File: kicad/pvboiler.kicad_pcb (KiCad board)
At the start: 2 copper layers, 125 x 60 mm, 52 parts, among them J1 Conn_01x04, J2 Screw_Terminal_01x04, J3 Conn_01x04, J4 Screw_Terminal_01x03, U1 MOC3021M, U2 H11AA1, U3 IRM-03-5

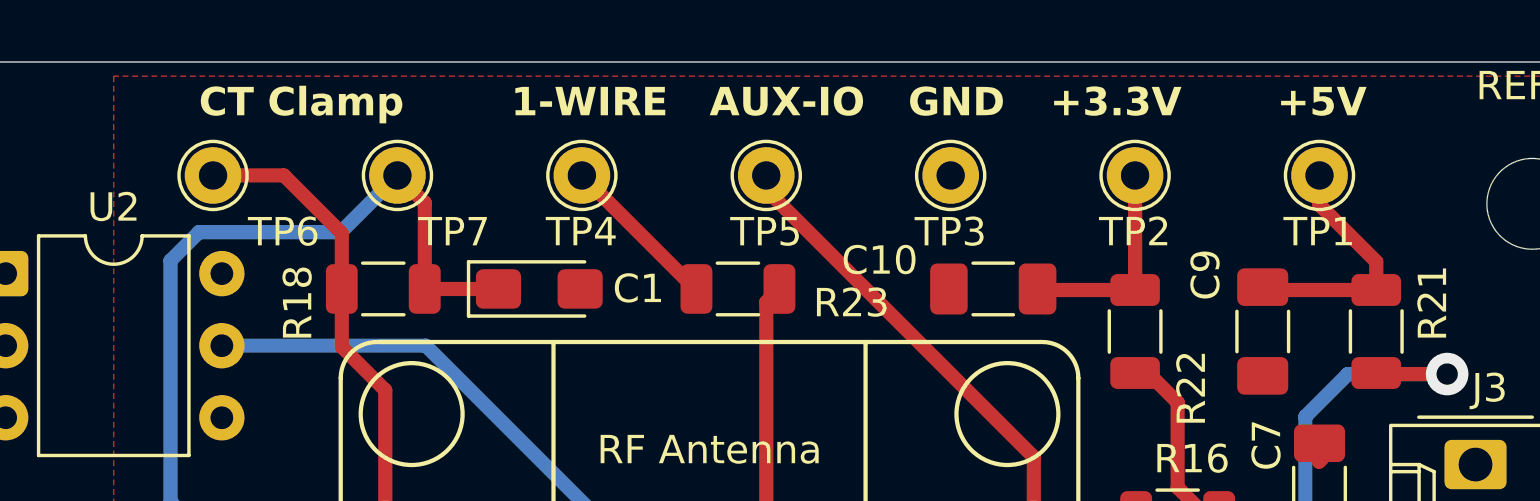
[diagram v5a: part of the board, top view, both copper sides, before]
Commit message: updated: Kicad schematic/pcb
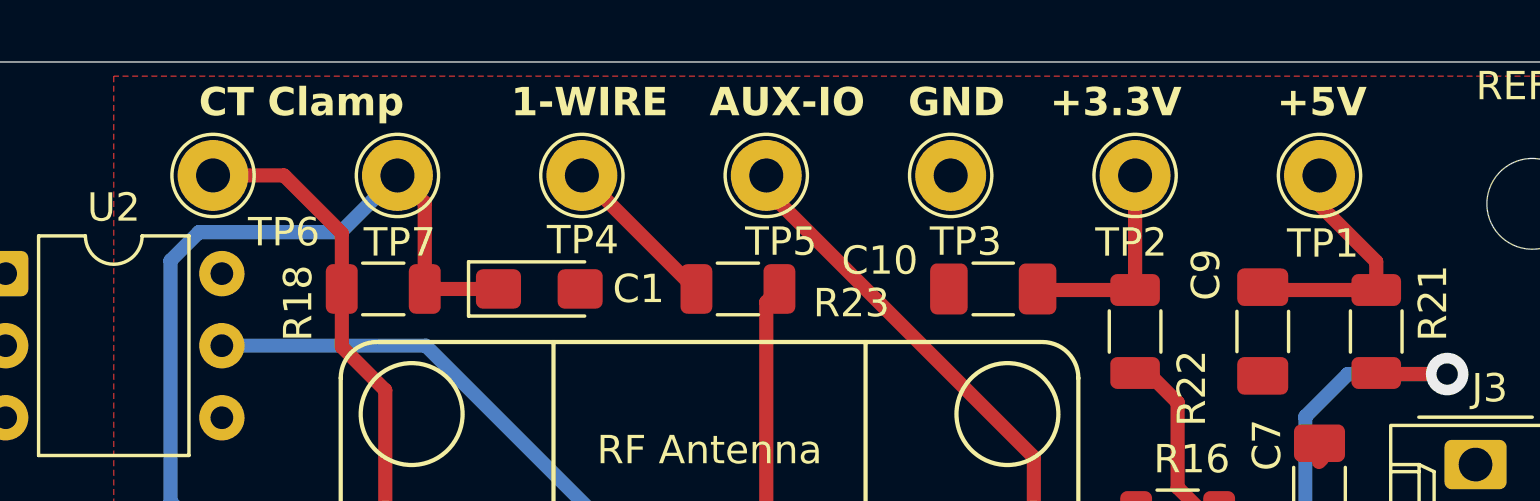
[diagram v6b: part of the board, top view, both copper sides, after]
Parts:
- R16: value 2K2 -> 10K
- TP1, TP2, TP3, TP4, TP5, TP6, TP7: footprint TestPoint:TestPoint_THTPad_D2.0mm_Drill1.0mm -> TestPoint:TestPoint_THTPad_D2.5mm_Drill1.2mm
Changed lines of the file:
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@@
 		)
 	)
-	(footprint "TestPoint:TestPoint_THTPad_D2.0mm_Drill1.0mm"
+	(footprint "TestPoint:TestPoint_THTPad_D2.5mm_Drill1.2mm"
 		(layer "F.Cu")
 		(at 114.5 39 180)
-		(descr "THT pad as test Point, diameter 2.0mm, hole diameter 1.0mm")
+		(descr "THT pad as test Point, diameter 2.5mm, hole diameter 1.2mm ")
 		(tags "test point THT pad")
 		(property "Reference" "TP3"
-			(at 0 -2 0)
+			(at -0.532554 -2.332656 180)
 			(layer "F.SilkS")
 			(effects
@@
 		)
 		(property "Value" "TestPoint"
-			(at 0 2.05 0)
+			(at 0 2.25 180)
 			(layer "F.Fab")
 			(effects
@@
 		(fp_circle
 			(center 0 0)
-			(end 0 1.2)
+			(end 0 1.45)
 			(stroke
 				(width 0.12)
@@
 		(fp_circle
 			(center 0 0)
-			(end 1.5 0)
+			(end 1.75 0)
 			(stroke
 				(width 0.05)
@@
 		)
 		(fp_text user "${REFERENCE}"
-			(at 0 -2 0)
+			(at 0 -2.15 180)
 			(layer "F.Fab")
 			(effects
@@
 		(pad "1" thru_hole circle
 			(at 0 0 180)
-			(size 2 2)
-			(drill 1)
+			(size 2.5 2.5)
+			(drill 1.2)
 			(layers "*.Cu" "*.Mask")
 			(remove_unused_layers no)
@@
 		(embedded_fonts no)
 	)
-	(footprint "TestPoint:TestPoint_THTPad_D2.0mm_Drill1.0mm"
+	(footprint "TestPoint:TestPoint_THTPad_D2.5mm_Drill1.2mm"
 		(layer "F.Cu")
 		(at 108 39)
-		(descr "THT pad as test Point, diameter 2.0mm, hole diameter 1.0mm")
+		(descr "THT pad as test Point, diameter 2.5mm, hole diameter 1.2mm ")
 		(tags "test point THT pad")
 		(property "Reference" "TP5"
-			(at 0 2 0)
+			(at 0.521976 2.332656 0)
 			(layer "F.SilkS")
 			(effects
@@
 		)
 		(property "Value" "TestPoint"
-			(at 0 2.05 0)
+			(at 0 2.25 0)
 			(layer "F.Fab")
 			(effects
@@
 		(fp_circle
 			(center 0 0)
-			(end 0 1.2)
+			(end 0 1.45)
 			(stroke
 				(width 0.12)
@@
 		(fp_circle
 			(center 0 0)
-			(end 1.5 0)
+			(end 1.75 0)
 			(stroke
 				(width 0.05)
@@
 		)
 		(fp_text user "${REFERENCE}"
-			(at 0 -2 0)
+			(at 0 -2.15 0)
 			(layer "F.Fab")
 			(effects
@@
 		(pad "1" thru_hole circle
 			(at 0 0)
-			(size 2 2)
-			(drill 1)
+			(size 2.5 2.5)
+			(drill 1.2)
 			(layers "*.Cu" "*.Mask")
 			(remove_unused_layers no)
@@
 		)
 	)
-	(footprint "TestPoint:TestPoint_THTPad_D2.0mm_Drill1.0mm"
+	(footprint "TestPoint:TestPoint_THTPad_D2.5mm_Drill1.2mm"
 		(layer "F.Cu")
 		(at 95 39)
-		(descr "THT pad as test Point, diameter 2.0mm, hole diameter 1.0mm")
+		(descr "THT pad as test Point, diameter 2.5mm, hole diameter 1.2mm ")
 		(tags "test point THT pad")
 		(property "Reference" "TP7"
-			(at 2 2 0)
+			(at 0.077367 2.359122 0)
 			(layer "F.SilkS")
 			(effects
@@
 		)
 		(property "Value" "TestPoint"
-			(at 0 2.05 0)
+			(at 0 2.25 0)
 			(layer "F.Fab")
 			(effects
@@
 		(fp_circle
 			(center 0 0)
-			(end 0 1.2)
+			(end 0 1.45)
 			(stroke
 				(width 0.12)
@@
 		(fp_circle
 			(center 0 0)
-			(end 1.5 0)
+			(end 1.75 0)
 			(stroke
 				(width 0.05)
@@
 		)
 		(fp_text user "${REFERENCE}"
-			(at 0 -2 0)
+			(at 0 -2.15 0)
 			(layer "F.Fab")
 			(effects
@@
 		(pad "1" thru_hole circle
 			(at 0 0)
-			(size 2 2)
-			(drill 1)
+			(size 2.5 2.5)
+			(drill 1.2)
 			(layers "*.Cu" "*.Mask")
 			(remove_unused_layers no)
@@
 		)
 	)
-	(footprint "TestPoint:TestPoint_THTPad_D2.0mm_Drill1.0mm"
+	(footprint "TestPoint:TestPoint_THTPad_D2.5mm_Drill1.2mm"
 		(layer "F.Cu")
 		(at 88.5 39)
-		(descr "THT pad as test Point, diameter 2.0mm, hole diameter 1.0mm")
+		(descr "THT pad as test Point, diameter 2.5mm, hole diameter 1.2mm ")
 		(tags "test point THT pad")
 		(property "Reference" "TP6"
@@
 		)
 		(property "Value" "TestPoint"
-			(at 0 2.05 0)
+			(at 0 2.25 0)
 			(layer "F.Fab")
 			(effects
@@
 		(fp_circle
 			(center 0 0)
-			(end 0 1.2)
+			(end 0 1.45)
 			(stroke
 				(width 0.12)
@@
 		(fp_circle
 			(center 0 0)
-			(end 1.5 0)
+			(end 1.75 0)
 			(stroke
 				(width 0.05)
@@
 		)
 		(fp_text user "${REFERENCE}"
-			(at 0 -2 0)
+			(at 0 -2.15 0)
 			(layer "F.Fab")
 			(effects
@@
 		(pad "1" thru_hole circle
 			(at 0 0)
-			(size 2 2)
-			(drill 1)
+			(size 2.5 2.5)
+			(drill 1.2)
 			(layers "*.Cu" "*.Mask")
 			(remove_unused_layers no)
@@
 			)
 		)
-		(property "Value" "2K2"
+		(property "Value" "10K"
 			(at 0 1.83 0)
 			(layer "F.Fab")
@@
 		)
 	)
-	(footprint "TestPoint:TestPoint_THTPad_D2.0mm_Drill1.0mm"
+	(footprint "TestPoint:TestPoint_THTPad_D2.5mm_Drill1.2mm"
 		(layer "F.Cu")
 		(at 127.5 39 180)
-		(descr "THT pad as test Point, diameter 2.0mm, hole diameter 1.0mm")
+		(descr "THT pad as test Point, diameter 2.5mm, hole diameter 1.2mm ")
 		(tags "test point THT pad")
 		(property "Reference" "TP1"
-			(at 0 -1.998 0)
+			(at -0.12214 -2.399836 180)
 			(layer "F.SilkS")
 			(effects
@@
 		)
 		(property "Value" "TestPoint"
-			(at 0 2.05 0)
+			(at 0 2.25 180)
 			(layer "F.Fab")
 			(effects
@@
 		(fp_circle
 			(center 0 0)
-			(end 0 1.2)
+			(end 0 1.45)
 			(stroke
 				(width 0.12)
@@
 		(fp_circle
 			(center 0 0)
-			(end 1.5 0)
+			(end 1.75 0)
 			(stroke
 				(width 0.05)
@@
 		)
 		(fp_text user "${REFERENCE}"
-			(at 0 -2 0)
+			(at 0 -2.15 180)
 			(layer "F.Fab")
 			(effects
@@
 		(pad "1" thru_hole circle
 			(at 0 0 180)
-			(size 2 2)
-			(drill 1)
+			(size 2.5 2.5)
+			(drill 1.2)
 			(layers "*.Cu" "*.Mask")
 			(remove_unused_layers no)
@@
 		)
 	)
-	(footprint "TestPoint:TestPoint_THTPad_D2.0mm_Drill1.0mm"
+	(footprint "TestPoint:TestPoint_THTPad_D2.5mm_Drill1.2mm"
 		(layer "F.Cu")
 		(at 101.5 39 180)
-		(descr "THT pad as test Point, diameter 2.0mm, hole diameter 1.0mm")
+		(descr "THT pad as test Point, diameter 2.5mm, hole diameter 1.2mm ")
 		(tags "test point THT pad")
 		(property "Reference" "TP4"
-			(at 0 -1.998 0)
+			(at -0.035014 -2.279725 180)
 			(layer "F.SilkS")
 			(effects
@@
 		)
 		(property "Value" "TestPoint"
-			(at 0 2.05 0)
+			(at 0 2.25 180)
 			(layer "F.Fab")
 			(effects
@@
 		(fp_circle
 			(center 0 0)
-			(end 0 1.2)
+			(end 0 1.45)
 			(stroke
 				(width 0.12)
@@
 		(fp_circle
 			(center 0 0)
-			(end 1.5 0)
+			(end 1.75 0)
 			(stroke
 				(width 0.05)
@@
 		)
 		(fp_text user "${REFERENCE}"
-			(at 0 -2 0)
+			(at 0 -2.15 180)
 			(layer "F.Fab")
 			(effects
@@
 		(pad "1" thru_hole circle
 			(at 0 0 180)
-			(size 2 2)
-			(drill 1)
+			(size 2.5 2.5)
+			(drill 1.2)
 			(layers "*.Cu" "*.Mask")
 			(remove_unused_layers no)
@@
 		)
 	)
-	(footprint "TestPoint:TestPoint_THTPad_D2.0mm_Drill1.0mm"
+	(footprint "TestPoint:TestPoint_THTPad_D2.5mm_Drill1.2mm"
 		(layer "F.Cu")
 		(at 121 39 180)
-		(descr "THT pad as test Point, diameter 2.0mm, hole diameter 1.0mm")
+		(descr "THT pad as test Point, diameter 2.5mm, hole diameter 1.2mm ")
 		(tags "test point THT pad")
 		(property "Reference" "TP2"
-			(at 0 -1.998 0)
+			(at 0.135452 -2.364548 180)
 			(layer "F.SilkS")
 			(effects
@@
 		)
 		(property "Value" "TestPoint"
-			(at 0 2.05 0)
+			(at 0 2.25 180)
 			(layer "F.Fab")
 			(effects
@@
 		(fp_circle
 			(center 0 0)
-			(end 0 1.2)
+			(end 0 1.45)
 			(stroke
 				(width 0.12)
@@
 		(fp_circle
 			(center 0 0)
-			(end 1.5 0)
+			(end 1.75 0)
 			(stroke
 				(width 0.05)
@@
 		)
 		(fp_text user "${REFERENCE}"
-			(at 0 -2 0)
+			(at 0 -2.15 180)
 			(layer "F.Fab")
 			(effects
@@
 		(pad "1" thru_hole circle
 			(at 0 0 180)
-			(size 2 2)
-			(drill 1)
+			(size 2.5 2.5)
+			(drill 1.2)
 			(layers "*.Cu" "*.Mask")
 			(remove_unused_layers no)
@@
 	)
 	(segment
+		(start 129.5 42.0375)
+		(end 129.5 43.0375)
+		(width 0.5)
+		(layer "F.Cu")
+		(net "Net-(C9-Pad1)")
+	)
+	(segment
+		(start 127.5 40.0375)
+		(end 129.5 42.0375)
+		(width 0.5)
+		(layer "F.Cu")
+		(net "Net-(C9-Pad1)")
+	)
+	(segment
+		(start 125.6 43.0375)
+		(end 125.5 42.9375)
+		(width 0.5)
+		(layer "F.Cu")
+		(net "Net-(C9-Pad1)")
+	)
+	(segment
+		(start 129.5 43.0375)
+		(end 125.6 43.0375)
+		(width 0.5)
+		(layer "F.Cu")
+		(net "Net-(C9-Pad1)")
+	)
+	(segment
+		(start 127.5 39)
+		(end 127.5 40.0375)
+		(width 0.5)
+		(layer "F.Cu")
+		(net "Net-(C9-Pad1)")
+	)
+	(segment
 		(start 133.9625 69.5)
 		(end 135.5 71.0375)
@@
 	)
 	(segment
-		(start 129.5 42.0375)
-		(end 129.5 43.0375)
-		(width 0.5)
-		(layer "F.Cu")
-		(net "Net-(C9-Pad1)")
-	)
-	(segment
-		(start 127.5 40.0375)
-		(end 129.5 42.0375)
-		(width 0.5)
-		(layer "F.Cu")
-		(net "Net-(C9-Pad1)")
-	)
-	(segment
-		(start 125.6 43.0375)
-		(end 125.5 42.9375)
-		(width 0.5)
-		(layer "F.Cu")
-		(net "Net-(C9-Pad1)")
-	)
-	(segment
-		(start 129.5 43.0375)
-		(end 125.6 43.0375)
+		(start 105.5 43)
+		(end 101.5 39)
 		(width 0.5)
 		(layer "F.Cu")
-		(net "Net-(C9-Pad1)")
+		(net "Net-(R23-Pad2)")
 	)
 	(segment
-		(start 127.5 39)
-		(end 127.5 40.0375)
+		(start 105.5375 43)
+		(end 105.5 43)
 		(width 0.5)
 		(layer "F.Cu")
-		(net "Net-(C9-Pad1)")
+		(net "Net-(R23-Pad2)")
 	)
 	(segment
@@
 		(net "Net-(C10-Pad1)")
 	)
-	(segment
-		(start 105.5 43)
-		(end 101.5 39)
-		(width 0.5)
-		(layer "F.Cu")
-		(net "Net-(R23-Pad2)")
-	)
-	(segment
-		(start 105.5375 43)
-		(end 105.5 43)
-		(width 0.5)
-		(layer "F.Cu")
-		(net "Net-(R23-Pad2)")
-	)
 	(zone
